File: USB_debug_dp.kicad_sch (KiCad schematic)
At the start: 120 parts, among them J3 USB-C_GCT_USB4105-GF-A, J4 USB-C_Amphenol_12401598E4, J9 Tag-Connect_TC2050-IDC-NL_2x5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, Q2 PJE138K, U13 TUSB1046-DCIRNQ, U15 AP22615A_TSOT26, U17 TPD4E05U06QDQARQ1, U18 TPD4E05U06QDQARQ1, U19 TPD4E05U06QDQARQ1, U20 TPD4E05U06QDQARQ1, U3 NTS0102_XSON, U4 FT230X_QFN, U4 NCP730BMT330_WSON, U8 TPS65988DHRSHR, U9 W25Q80DV_USON

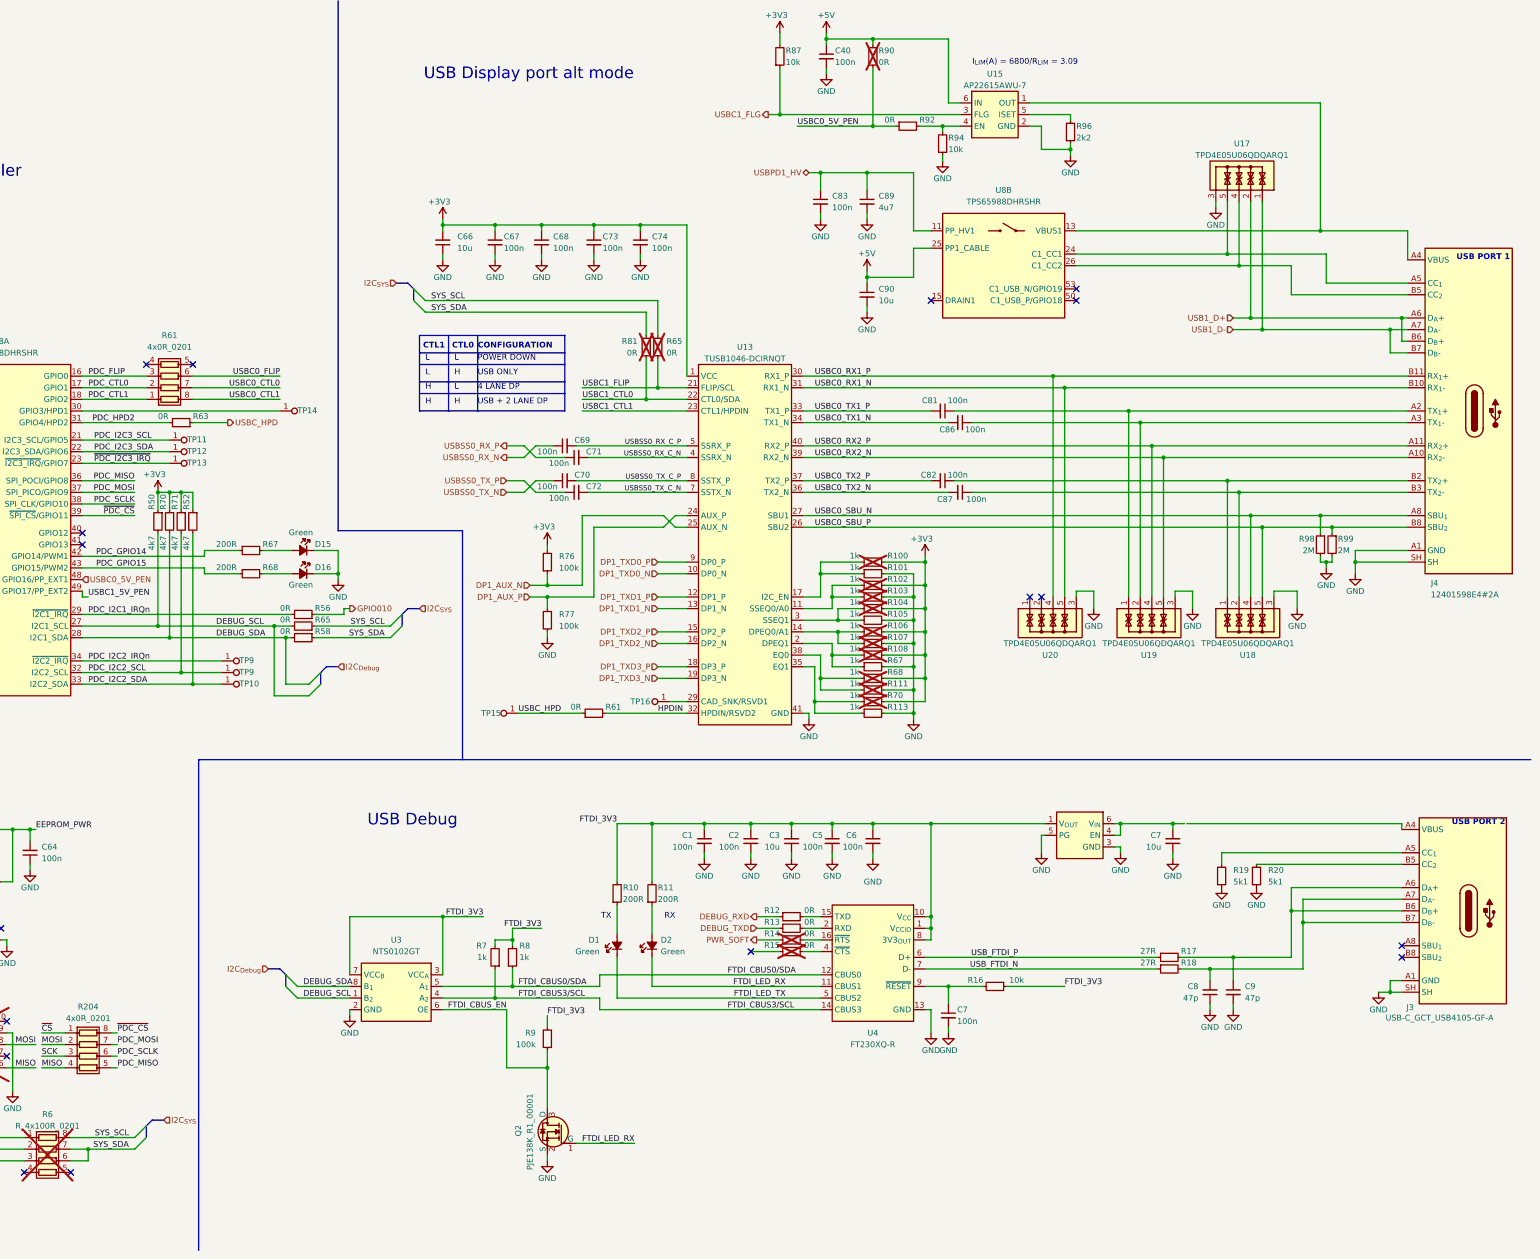
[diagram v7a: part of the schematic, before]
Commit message: [#82055] Revert back to USB-PD on DP and Debug ports
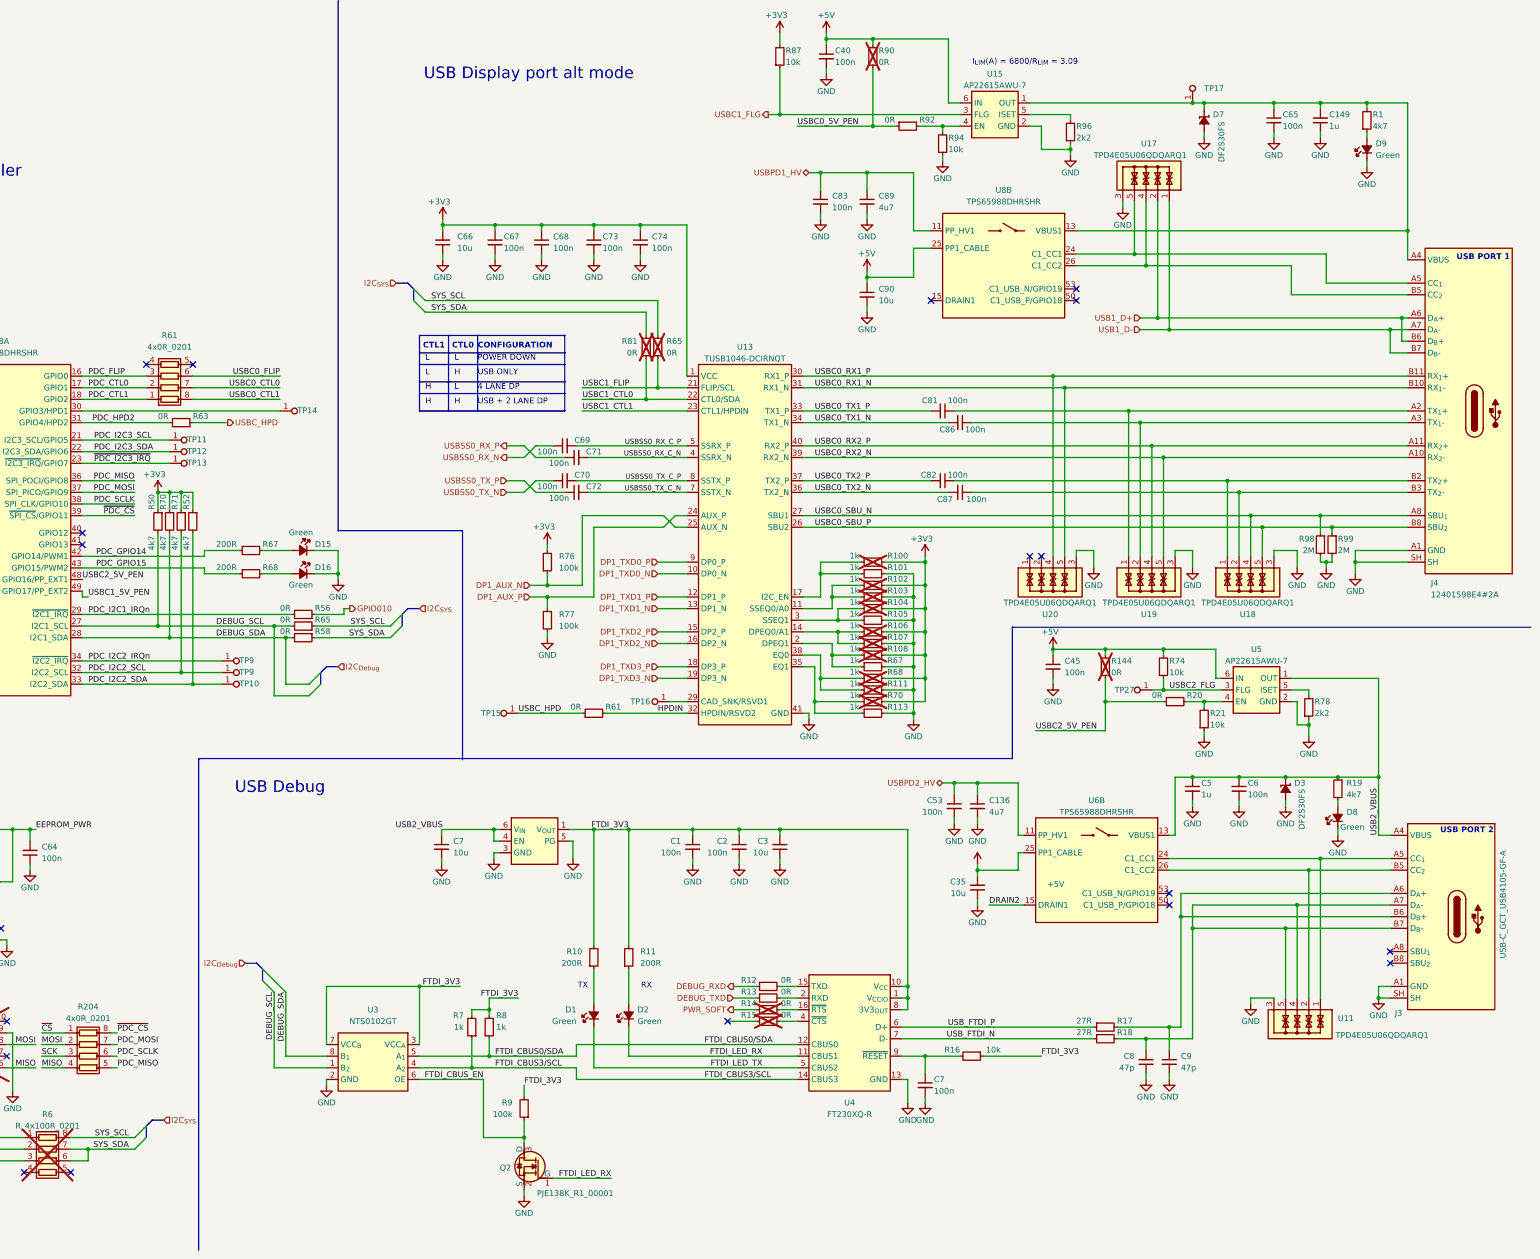
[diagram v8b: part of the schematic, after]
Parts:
- removed C5: C_100n_0402, antmicro-footprints:C_0402_1005Metric, symbol antmicroCapacitors0402:C_100n_0402
- removed R19, R20: R_5k1_0402, antmicro-footprints:R_0402_1005Metric, symbol antmicroResistors0402:R_5k1_0402
- added C136: C_4u7_25V_0402, antmicro-footprints:C_0402_1005Metric, symbol antmicroCapacitors0402:C_4u7_25V_0402
- added C149, C5: C_1u_25V_0402, antmicro-footprints:C_0402_1005Metric, symbol antmicroCapacitors0402:C_1u_25V_0402
- added C35: C_10u_0402, antmicro-footprints:C_0402_1005Metric, symbol antmicroCapacitors0402:C_10u_0402
- added C45, C53, C65: C_100n_0402, antmicro-footprints:C_0402_1005Metric, symbol antmicroCapacitors0402:C_100n_0402
- added D3, D7: DF2S30FS_SOD, antmicro-footprints:SOD-923, symbol antmicroTVSDiodes:DF2S30FS_SOD
- added D8, D9: LED_G_0603_LTST-C190GKT, antmicro-footprints:LED_0603_1608Metric_G, symbol antmicroLEDIndicationDiscrete:LED_G_0603_LTST-C190GKT
- added R1, R19: R_4k7_0402, antmicro-footprints:R_0402_1005Metric, symbol antmicroResistors0402:R_4k7_0402
- added R144, R20: R_0R_0402, antmicro-footprints:R_0402_1005Metric, symbol antmicroResistors0402:R_0R_0402
- added R21, R74: R_10k_0402, antmicro-footprints:R_0402_1005Metric, symbol antmicroResistors0402:R_10k_0402
- added R78: R_2k2_0402, antmicro-footprints:R_0402_1005Metric, symbol antmicroResistors0402:R_2k2_0402
- added TP17, TP27: TP_0.75mm_SMD, antmicro-footprints:TP_SMD_0.75mm, symbol antmicroTestPoints:TP_0.75mm_SMD
- added U11: TPD4E05U06QDQARQ1, antmicro-footprints:USON-10_2.5x1mm_P0.5mm, symbol antmicroTVSDiodes:TPD4E05U06QDQARQ1
- added U5: AP22615A_TSOT26, antmicro-footprints:TSOT23-6, symbol antmicroPMICPowerDistributionSwitchesLoadDrivers:AP22615A_TSOT26
- added U6: TPS65988DHRSHR, antmicro-footprints:IC_TPS65987DDHRSHR, symbol antmicroInterfaceControllers:TPS65988DHRSHR
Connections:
- net +5V: now also C35.2, C45.1, R144.2, R74.2, U5.6 (IN), U6.25 (PP1_CABLE)
- net FTDI_3V3: no longer C6.1
- net GND: now also C136.2, C149.1, C35.1, C45.2, C5.2, C53.2, C65.2, D3.2 (A), D7.2 (A), D8.1 (C), D9.1 (C), R21.1, R78.1, U11.3, U11.8, U5.2 (GND)
- net USBC0_5V_PEN: no longer U8.48 (GPIO16/PP_EXT1)
- net at C8.2, J3.A7 (D_{A}-), J3.B7 (D_{B}-)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: now also U11.4, U11.5, U11.6, U11.7
- net at J3.B5 (CC_{2}): now also U11.2, U11.9, U6.26 (C1_CC2)
- net USB2_VBUS: now reaches C7.1, U4.4 (EN), U4.6 (V_{IN})
- net USB2_VBUS: now also C6.1, J3.A4 (VBUS), J3.A9 (VBUS), J3.B4 (VBUS), J3.B9 (VBUS), C5.1, D3.1 (C), R19.1, U5.1 (OUT), U6.13 (VBUS1)
- net at J4.A4 (VBUS), J4.A9 (VBUS), J4.B4 (VBUS)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: now also C149.2, C65.1, D7.1 (C), R1.2, TP17.1
- net at J3.A5 (CC_{1}): now also U11.1, U11.10, U6.24 (C1_CC1)
- new net: R20.2, R21.2, U5.4 (EN)
- new net: D8.2 (A), R19.2
- new net: D9.2 (A), R1.1
- new net: R78.2, U5.5 (ISET)
- new net DRAIN2: U6.15 (DRAIN1), U6.19 (DRAIN1), U6.58 (DRAIN1), U6.8 (DRAIN1)
- new net USBC2_5V_PEN: R144.1, R20.1, U8.48 (GPIO16/PP_EXT1)
- new net USBC2_FLG: R74.1, TP27.1, U5.3 (FLG)
- new net USBPD2_HV: C136.1, C53.1, U6.11 (PP_HV1)
- no-connect marks 17 -> 19
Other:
- moved on the sheet: C1, C2, C3, C7, C8, C9, D1, D2, J3, Q2, R10, R11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
